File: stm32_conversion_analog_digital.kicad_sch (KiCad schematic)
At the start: 38 parts, among them U1 MCP6004, U2 MCP6004, U3 MCP6002-xMS, U8 MCP6004

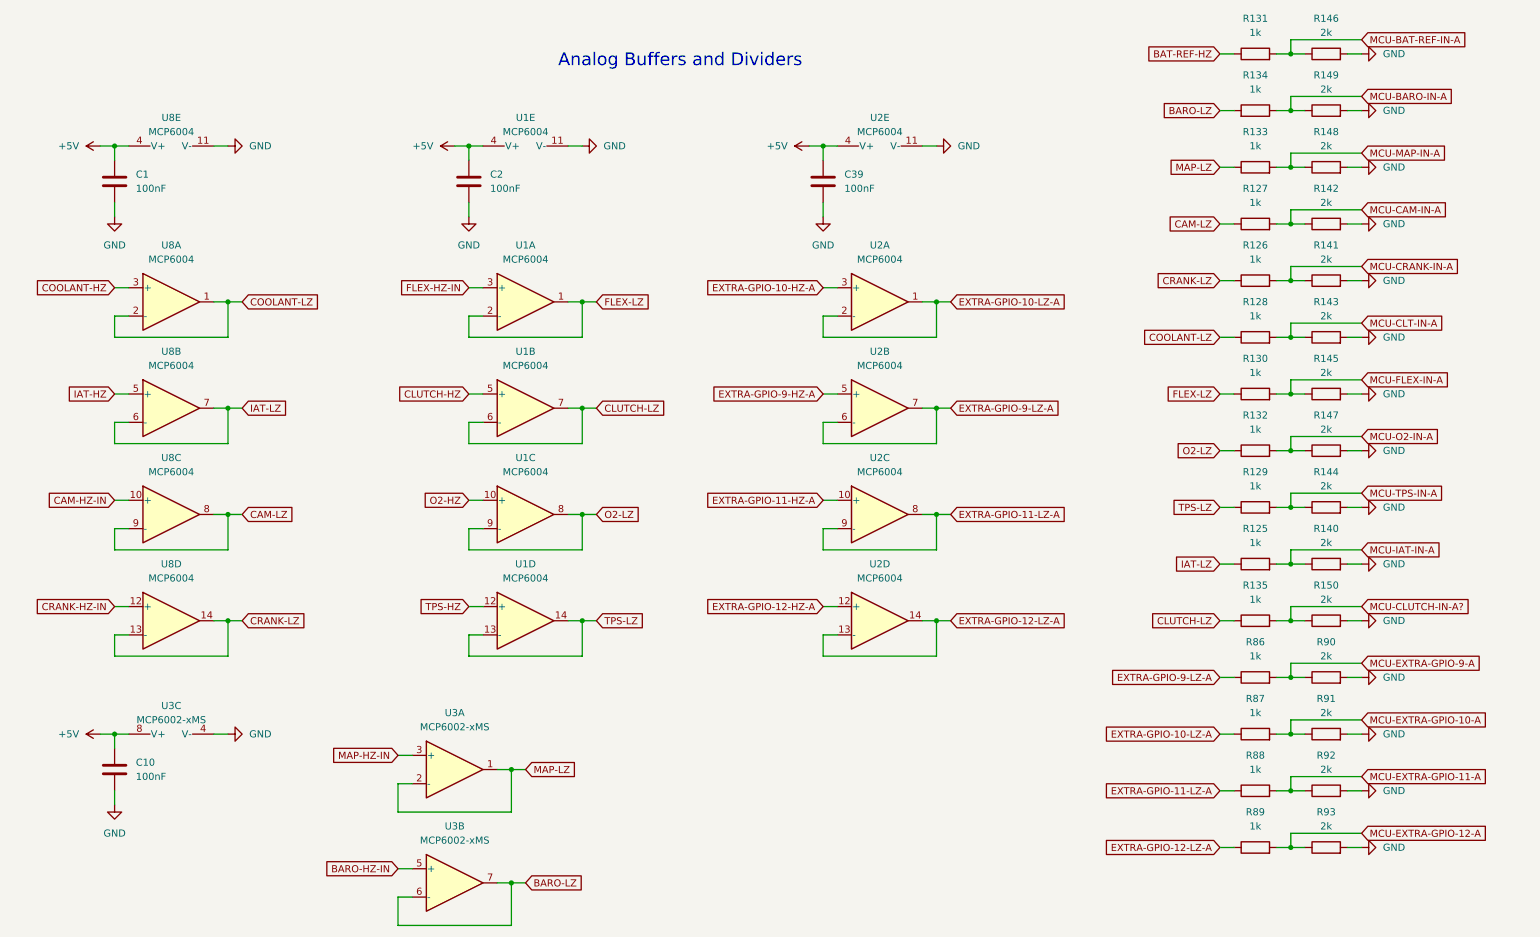
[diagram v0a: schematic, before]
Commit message: Updated reference layout
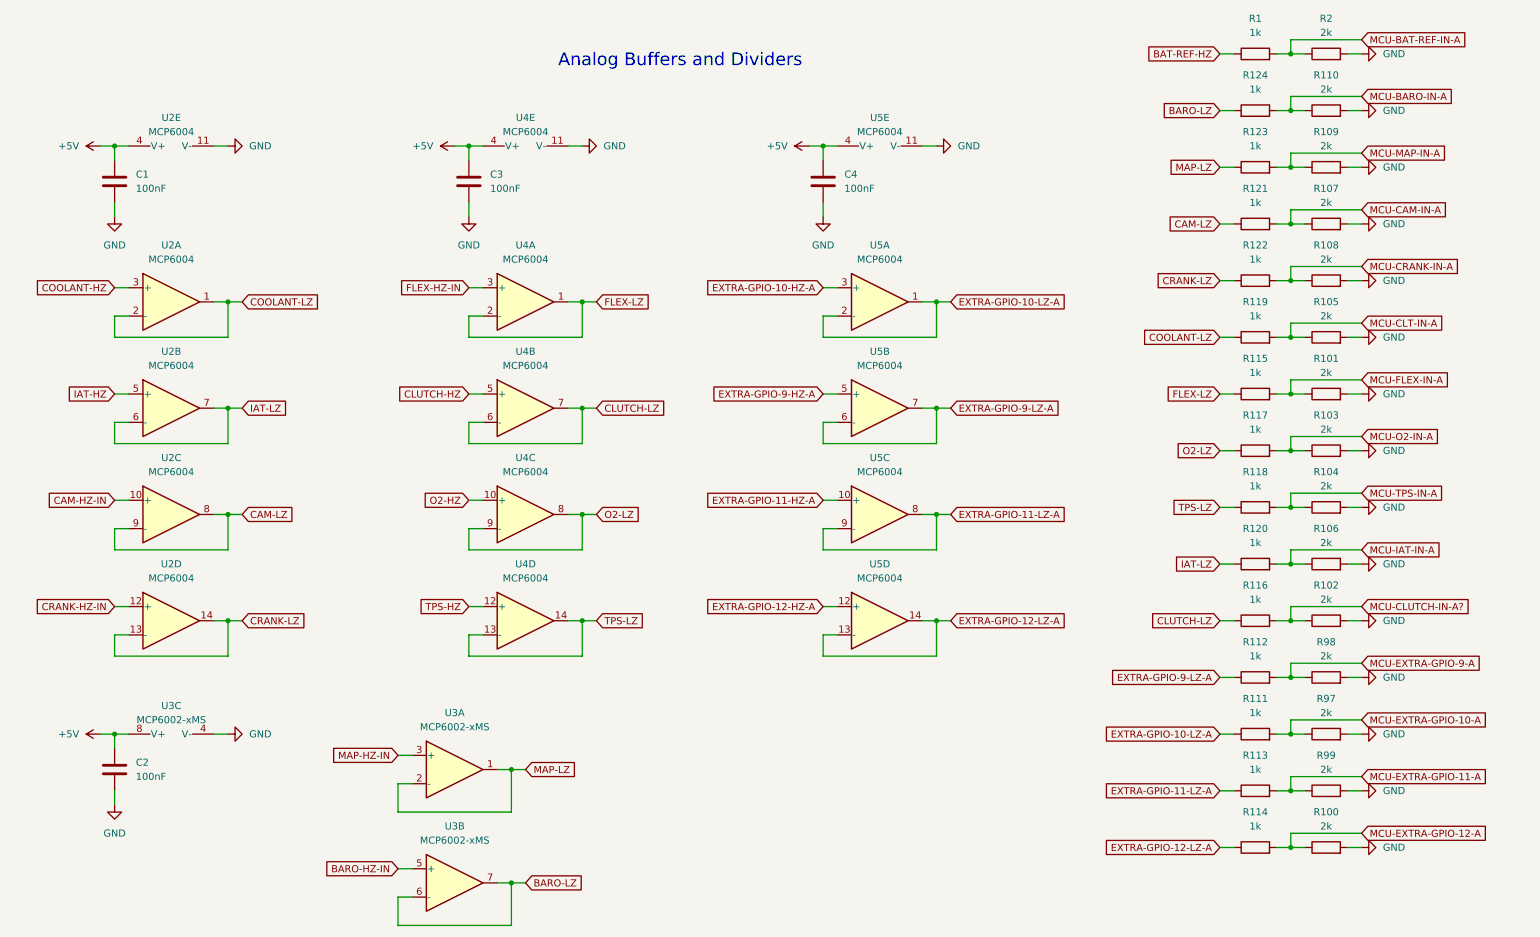
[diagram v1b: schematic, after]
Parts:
- renumbered C10 to C2, C2 to C3, C39 to C4, R131 to R1, R93 to R100, R145 to R101, R150 to R102, R147 to R103, R144 to R104, R143 to R105, R140 to R106, R142 to R107, R141 to R108, R148 to R109, R149 to R110, R87 to R111, R86 to R112, R88 to R113, R89 to R114, R130 to R115, R135 to R116, R132 to R117, R129 to R118, R128 to R119, R125 to R120, R127 to R121, R126 to R122, R133 to R123, R134 to R124, R146 to R2, R91 to R97, R90 to R98, R92 to R99, U8 to U2, U1 to U4, U2 to U5
